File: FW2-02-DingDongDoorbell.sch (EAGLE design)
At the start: 12 parts, among them IC1 LM555N

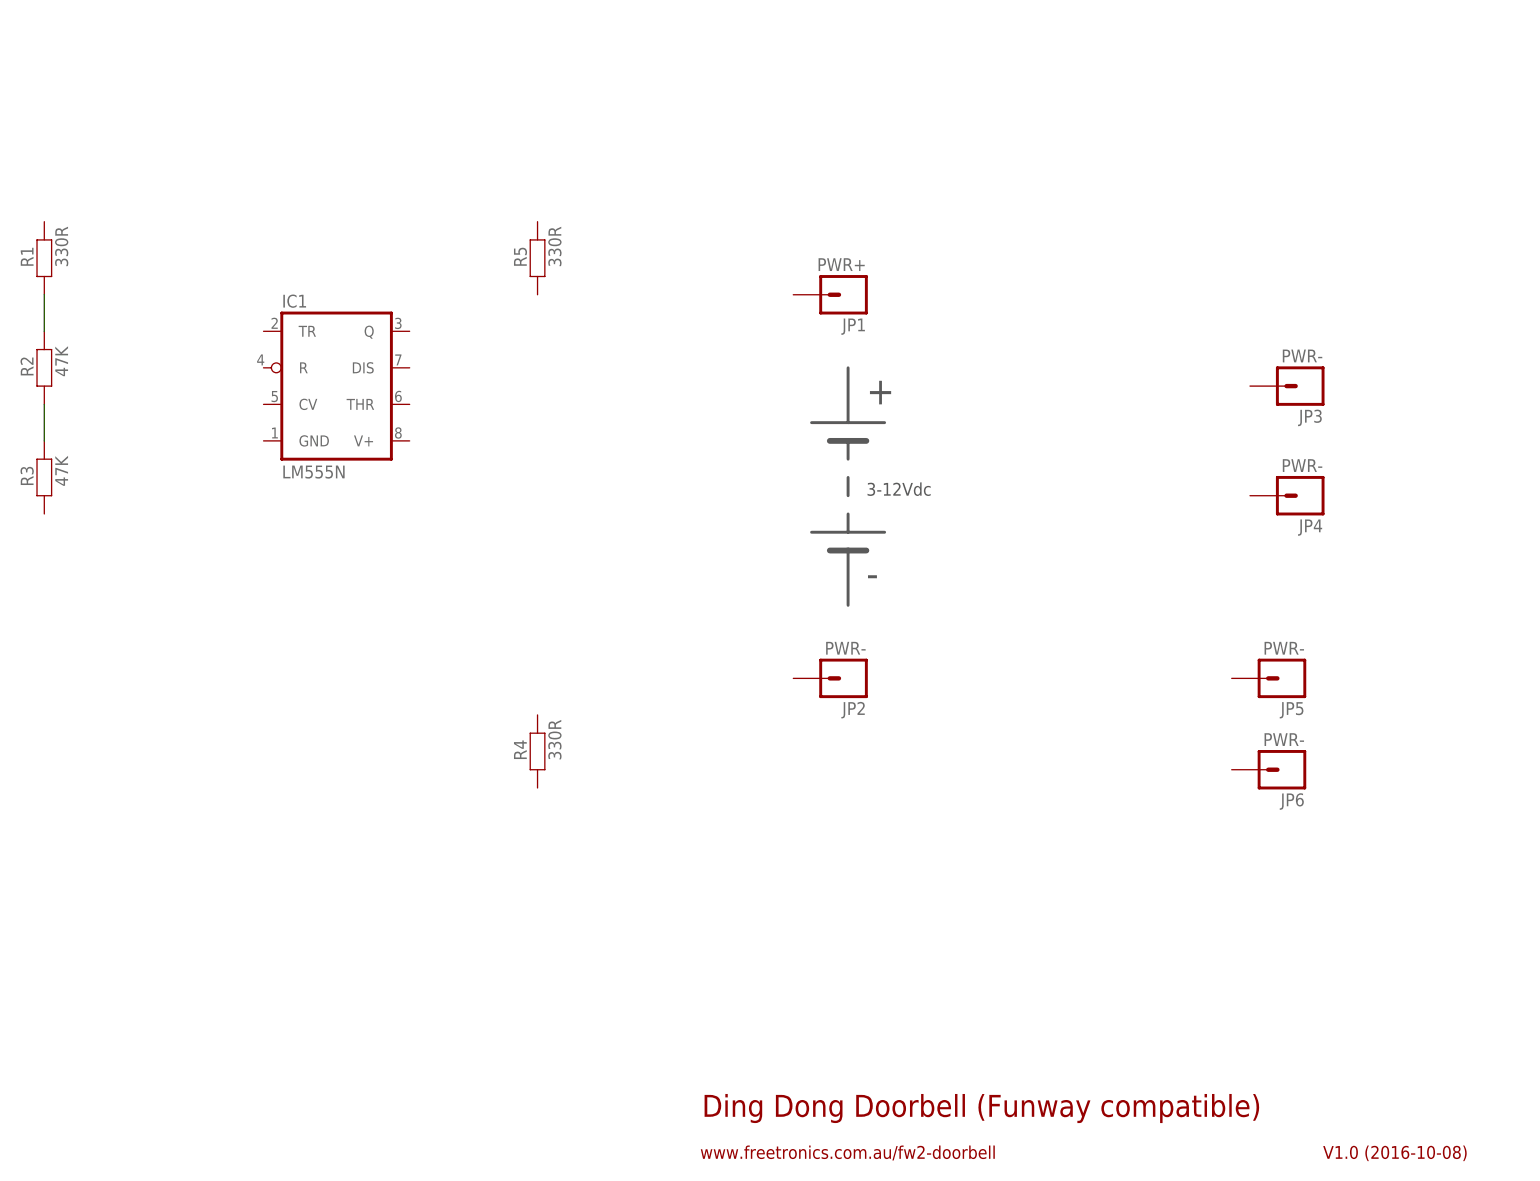
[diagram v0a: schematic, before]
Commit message: Most of the schematic done, base part positions
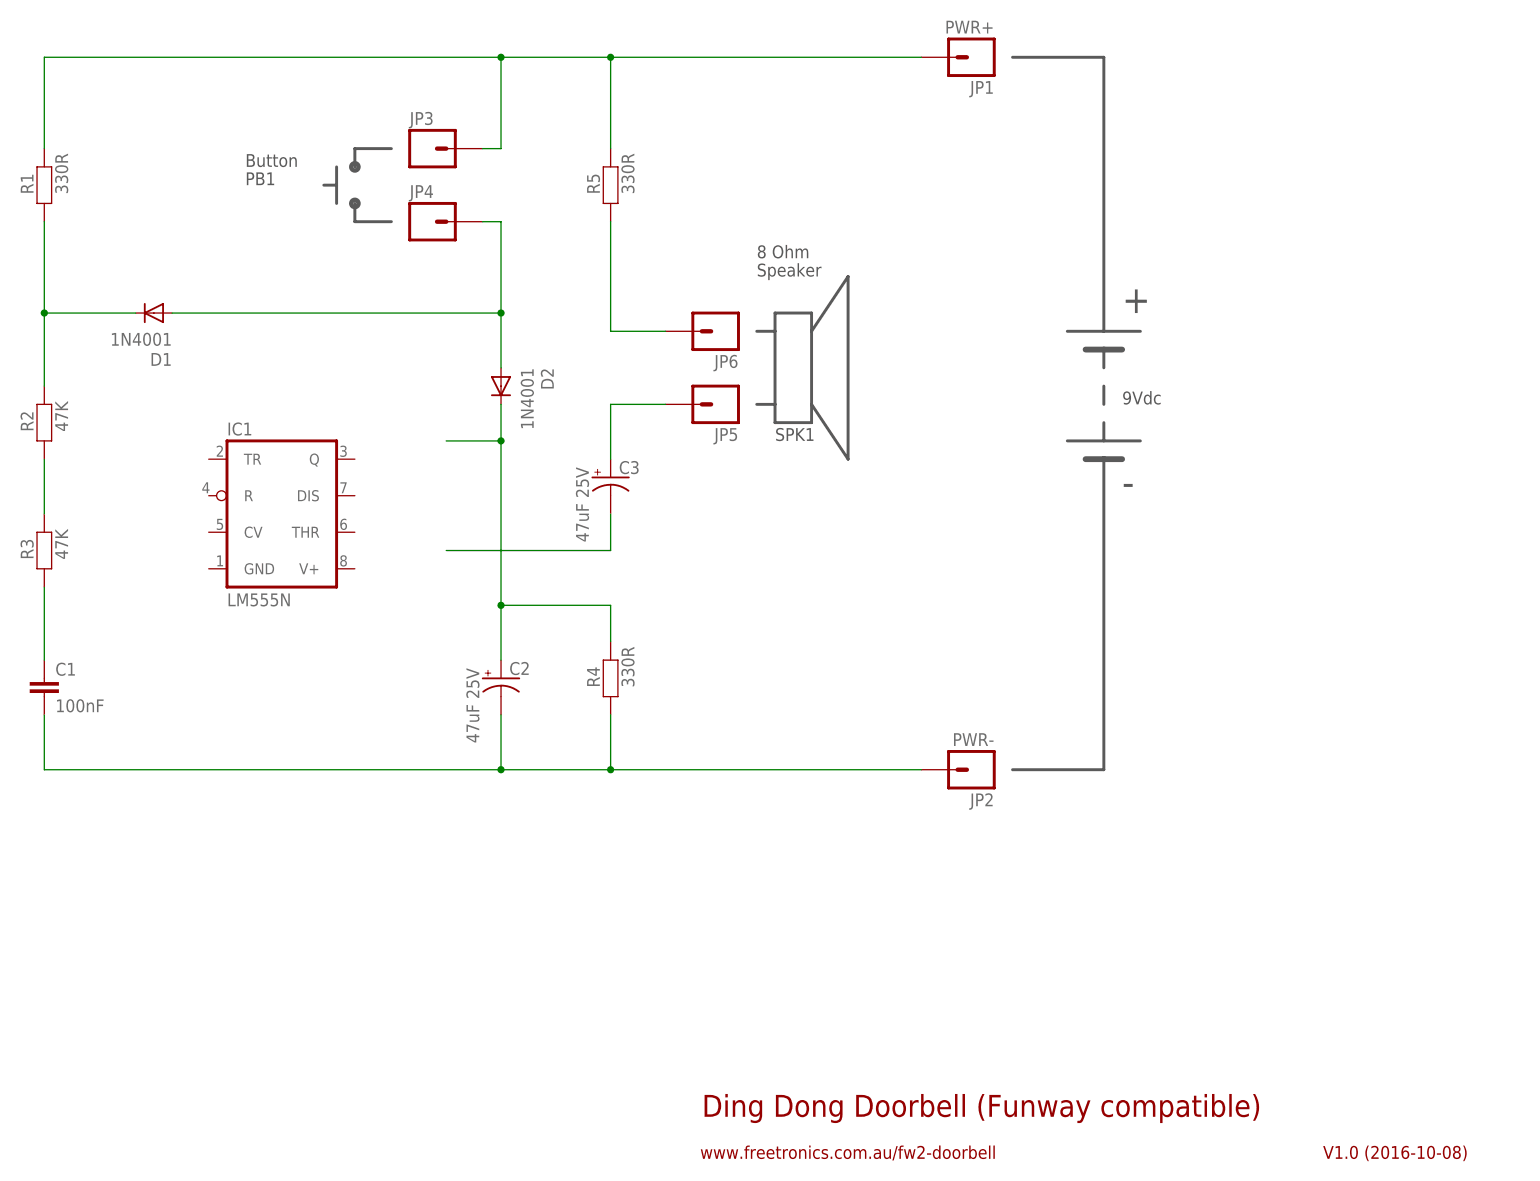
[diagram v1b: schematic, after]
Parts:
- added C1: 100nF, freetronics-2:CAPPTH
- added C2, C3: 47uF 25V, freetronics-jon.1:CAP_POLPTH2
- added D1, D2: 1N4001, freetronics-2:DIODEPTH
- JP5: value PWR- -> SPKR-
- JP6: value PWR- -> SPKR+
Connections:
- new net N$10: C1.2, C2.-, JP2.1, R4.1
- new net N$11: C1.1, R3.1
- new net N$3: D1.A, D2.A, JP4.1
- new net N$4: JP1.1, JP3.1, R1.2, R5.2
- new net N$5: JP6.1, R5.1
- new net N$6: C3.+, JP5.1
- new net N$7: C3.-
- new net N$8: C2.+, D2.C, R4.2
- net N$1: now also D1.C
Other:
- note added: "8 Ohm"
- note added: "9Vdc"
- note added: "Button"
- note added: "PB1"
- note added: "SPK1"
- note added: "Speaker"
- note removed: "3-12Vdc"
- moved on the sheet: IC1, JP1, JP2, JP3, JP4, JP5, JP6, R1, R2, R3, R4, R5

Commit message: Modified 555 symbol to match original; basic PCB routing
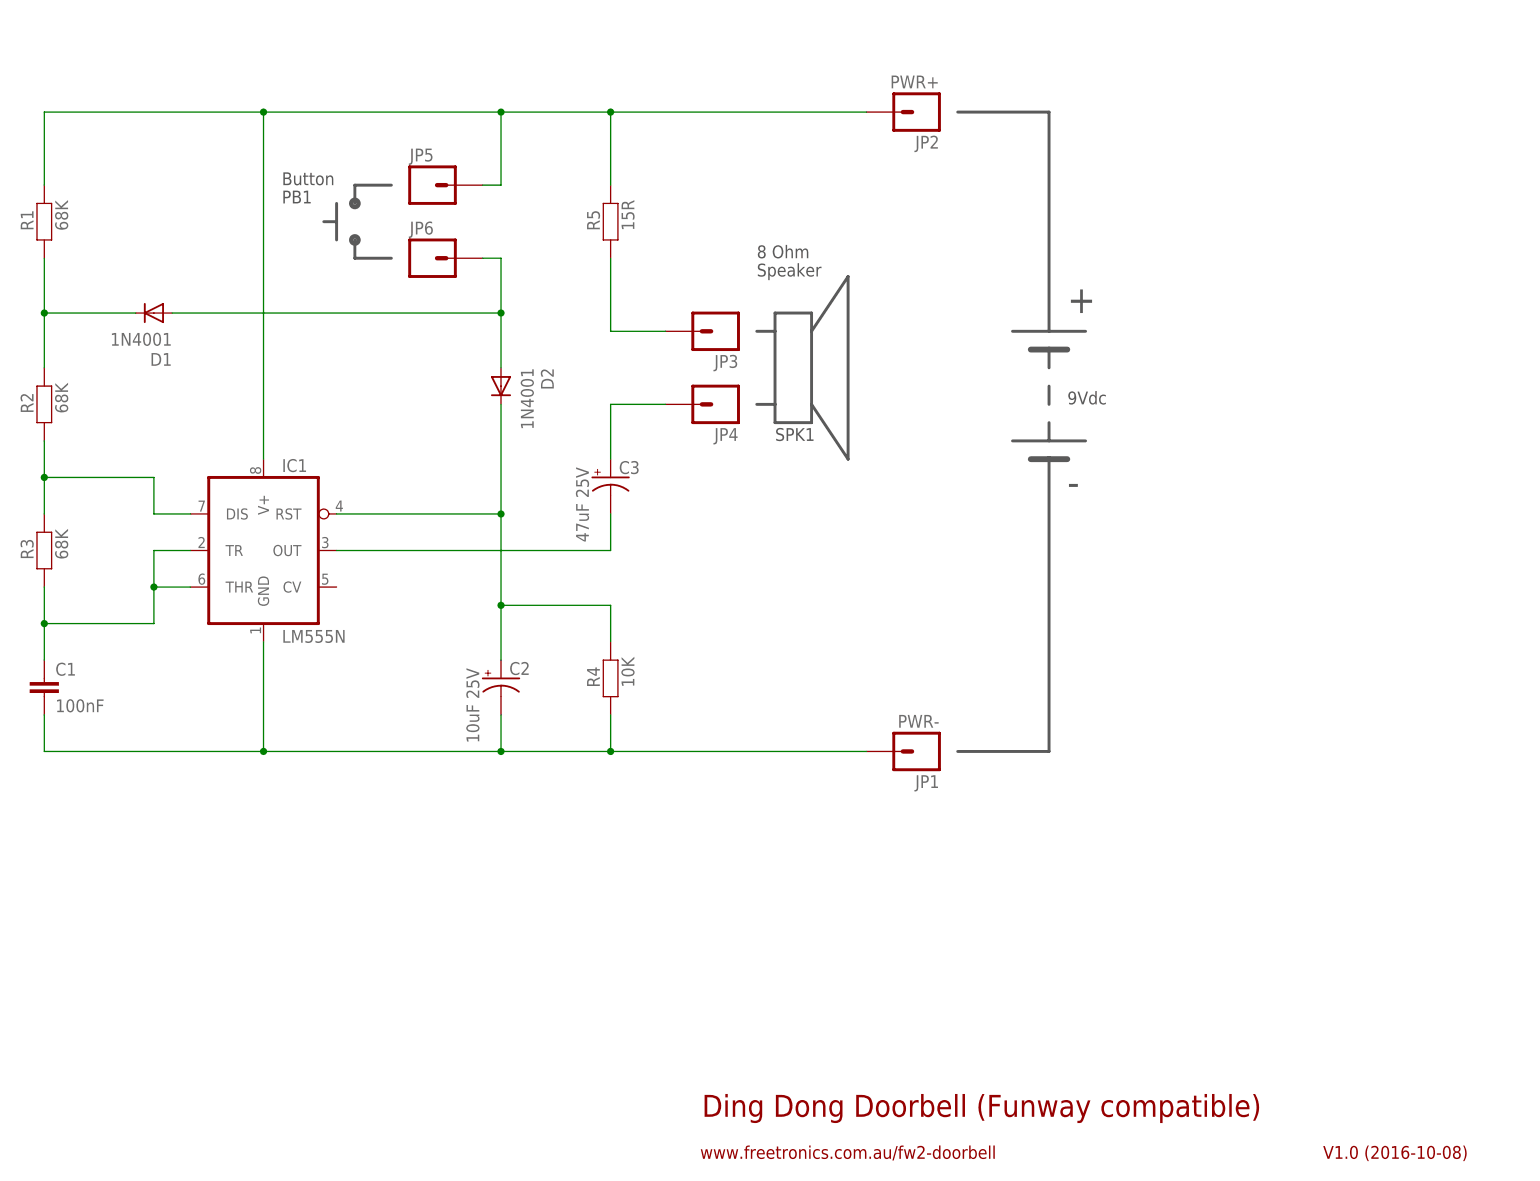
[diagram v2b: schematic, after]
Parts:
- C2: value 47uF 25V -> 10uF 25V
- IC1: device linear:LM555N -> freetronics-jon:LM555N
- JP1: value PWR+ -> PWR-
- JP2: value PWR- -> PWR+
- JP3: value PWR- -> SPKR+
- JP4: value PWR- -> SPKR-
- JP5: value SPKR- -> PWR-
- JP6: value SPKR+ -> PWR-
- R1: value 330R -> 68K
- R2, R3: value 47K -> 68K
- R4: value 330R -> 10K
- R5: value 330R -> 15R
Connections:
- removed net N$11: C1.1, R3.1
- new net N$12: C1.1, IC1.THR, IC1.TR, R3.1
- net N$10: now also IC1.GND, JP1.1; no longer JP2.1
- net N$2: now also IC1.DIS
- net N$3: now also JP6.1; no longer JP4.1
- net N$4: now also IC1.V+, JP2.1, JP5.1; no longer JP1.1, JP3.1
- net N$5: now also JP3.1; no longer JP6.1
- net N$6: now also JP4.1; no longer JP5.1
- net N$7: now also IC1.OUT
- net N$8: now also IC1.RST
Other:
- moved on the sheet: IC1, JP1, JP2, JP3, JP4, JP5, JP6, R1, R2, R5

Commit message: Updated silkscreen and labels
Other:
- note added: "Ding Dong Doorbell (Fun Way compatible)"
- note removed: "Ding Dong Doorbell (Funway compatible)"
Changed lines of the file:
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@@
 <sheet>
 <plain>
-<text x="129.54" y="12.7" size="3.048" layer="94">Ding Dong Doorbell (Funway compatible)</text>
+<text x="129.54" y="12.7" size="3.048" layer="94">Ding Dong Doorbell (Fun Way compatible)</text>
 <text x="215.9" y="6.858" size="1.778" layer="94">V1.0 (2016-10-08)</text>
 <text x="129.286" y="6.858" size="1.778" layer="94">www.freetronics.com.au/fw2-doorbell</text>

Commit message: Increased pad sizes; improved silkscreen
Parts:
- C2: value 10uF 25V -> 10uF
- C3: value 47uF 25V -> 47uF
- IC1: value LM555N -> 555L; device freetronics-jon:LM555N -> freetronics-jon:555L
- R1, R2, R3, R4, R5: device freetronics:FREETRONICS_RESISTORPTH2 -> freetronics:FREETRONICS_RESISTORPTH3
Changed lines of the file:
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@@
 <part name="JP2" library="freetronics-master-v1.1" deviceset="M01" device="PTH" value="PWR+"/>
 <part name="JP1" library="freetronics-master-v1.1" deviceset="M01" device="PTH" value="PWR-"/>
-<part name="R1" library="freetronics" deviceset="FREETRONICS_RESISTOR" device="PTH2" value="68K"/>
-<part name="R2" library="freetronics" deviceset="FREETRONICS_RESISTOR" device="PTH2" value="68K"/>
-<part name="R3" library="freetronics" deviceset="FREETRONICS_RESISTOR" device="PTH2" value="68K"/>
-<part name="R4" library="freetronics" deviceset="FREETRONICS_RESISTOR" device="PTH2" value="10K"/>
-<part name="R5" library="freetronics" deviceset="FREETRONICS_RESISTOR" device="PTH2" value="15R"/>
+<part name="R1" library="freetronics" deviceset="FREETRONICS_RESISTOR" device="PTH3" value="68K"/>
+<part name="R2" library="freetronics" deviceset="FREETRONICS_RESISTOR" device="PTH3" value="68K"/>
+<part name="R3" library="freetronics" deviceset="FREETRONICS_RESISTOR" device="PTH3" value="68K"/>
+<part name="R4" library="freetronics" deviceset="FREETRONICS_RESISTOR" device="PTH3" value="10K"/>
+<part name="R5" library="freetronics" deviceset="FREETRONICS_RESISTOR" device="PTH3" value="15R"/>
 <part name="JP5" library="freetronics-master-v1.1" deviceset="M01" device="PTH" value="PWR-"/>
 <part name="JP6" library="freetronics-master-v1.1" deviceset="M01" device="PTH" value="PWR-"/>
@@
 <part name="D1" library="freetronics-2" deviceset="DIODE" device="PTH" value="1N4001"/>
 <part name="C1" library="freetronics-2" deviceset="CAP" device="PTH" value="100nF"/>
-<part name="C3" library="freetronics-jon.1" deviceset="CAP_POL" device="PTH2" value="47uF 25V"/>
+<part name="C3" library="freetronics-jon.1" deviceset="CAP_POL" device="PTH2" value="47uF"/>
 <part name="D2" library="freetronics-2" deviceset="DIODE" device="PTH" value="1N4001"/>
-<part name="C2" library="freetronics-jon.1" deviceset="CAP_POL" device="PTH2" value="10uF 25V"/>
-<part name="IC1" library="freetronics-jon" deviceset="*555" device="N" technology="LM"/>
+<part name="C2" library="freetronics-jon.1" deviceset="CAP_POL" device="PTH2" value="10uF"/>
+<part name="IC1" library="freetronics-jon" deviceset="*555" device="L" value="555L"/>
 </parts>
 <sheets>
@@
 </sheet>
 </sheets>
+<errors>
+</errors>
 </schematic>
 </drawing>
